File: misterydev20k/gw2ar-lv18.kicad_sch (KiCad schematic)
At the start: 53 parts, among them J3 Jumper block, U11 LY68L6400SLIT, U5 GW2AR-LV18-QN88, U6 W25Q128JVS, U8 SY8113BADC, Y2 27MHz

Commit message: More small pcb updates
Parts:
- added C62, C63, C64: 100nF, Capacitor_SMD:C_0402_1005Metric, symbol Device:C_Small
- added C65, C66, C67, C68: 100nF, Capacitor_SMD:C_0603_1608Metric, symbol Device:C_Small
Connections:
- net +1V0: now also C62.1, C63.2, C64.2, C65.1, C66.1
- net +3.3V: now also C67.1, C68.1
- net GND: now also C62.2, C63.1, C64.1, C65.2, C66.2, C67.2, C68.2
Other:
- moved on the sheet: C33, C34, C35, C36, C37, C38, C39, C4, C46, C47, C48, C49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

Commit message: Fix FPGA orientation in production files
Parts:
- C65, C66, C67, C68: now left out of the parts list
- U5: FT Rotation Offset (none) -> 270
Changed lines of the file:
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@@
 			)
 		)
+		(property "FT Rotation Offset" "270"
+			(at 144.78 88.9 0)
+			(effects
+				(font
+					(size 1.27 1.27)
+				)
+				(hide yes)
+			)
+		)
 		(pin "74"
 		)
@@
 		(unit 1)
 		(exclude_from_sim no)
-		(in_bom yes)
+		(in_bom no)
 		(on_board yes)
 		(dnp yes)
@@
 		(unit 1)
 		(exclude_from_sim no)
-		(in_bom yes)
+		(in_bom no)
 		(on_board yes)
 		(dnp yes)
@@
 		(unit 1)
 		(exclude_from_sim no)
-		(in_bom yes)
+		(in_bom no)
 		(on_board yes)
 		(dnp yes)
@@
 		(unit 1)
 		(exclude_from_sim no)
-		(in_bom yes)
+		(in_bom no)
 		(on_board yes)
 		(dnp yes)

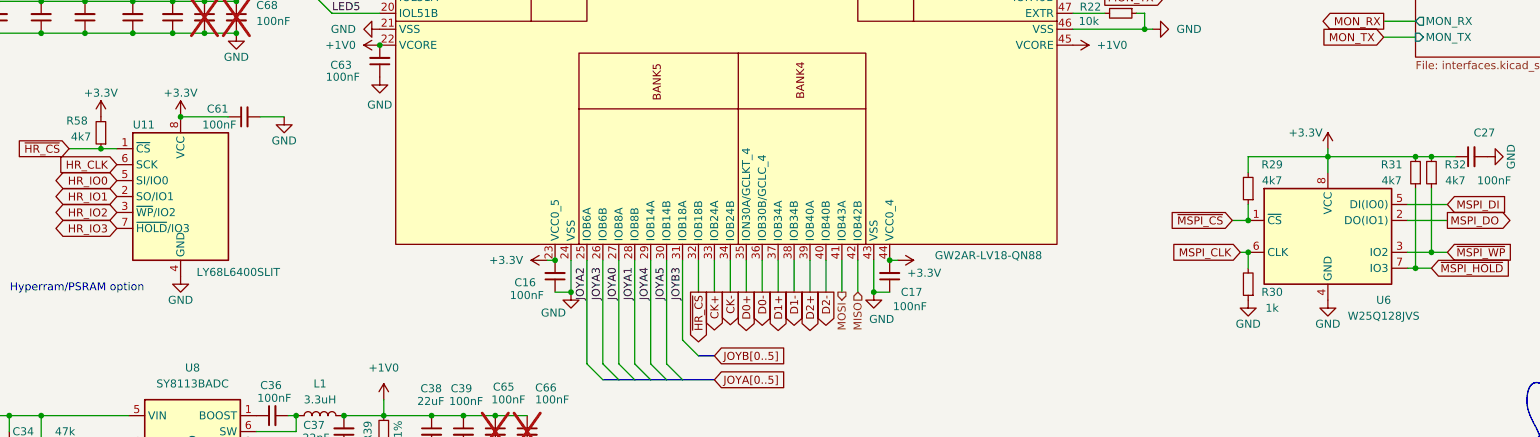
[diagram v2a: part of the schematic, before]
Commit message: Update misterydev20k to v1.1
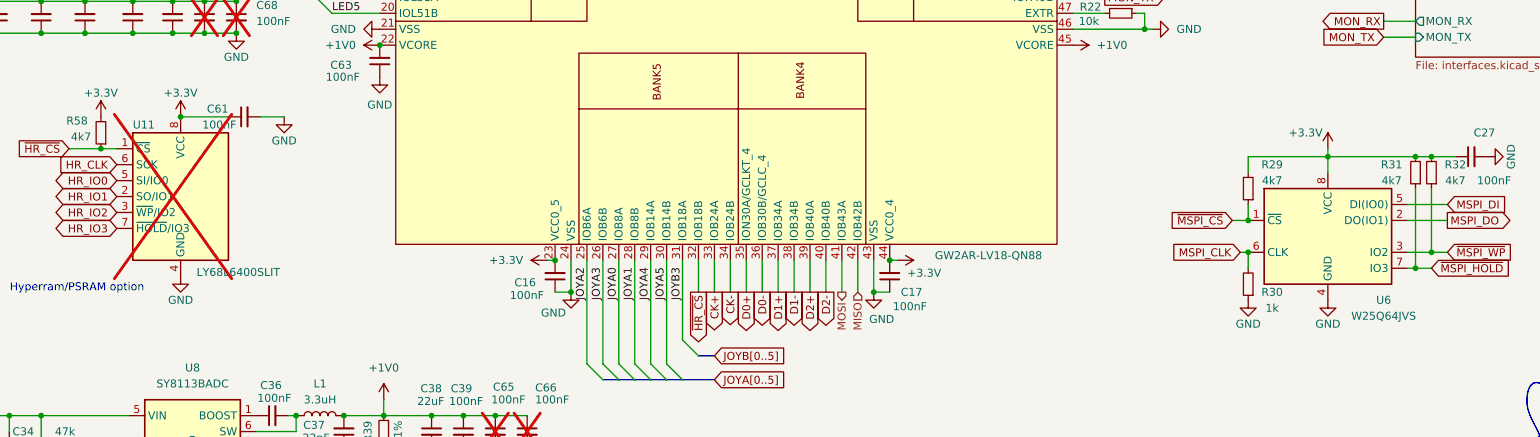
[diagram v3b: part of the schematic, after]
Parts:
- U11: now not fitted; now left out of the parts list
- U6: value W25Q128JVS -> W25Q64JVS; LCSC Part # C131025 -> C179171
